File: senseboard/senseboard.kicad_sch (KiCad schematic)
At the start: 5 parts, among them U1 STM32L4Q5CGUx, U2 SHT4x, U3 SCD41-D-R2, U4 SGP41-D-R4, U5 TPS62840YBGR

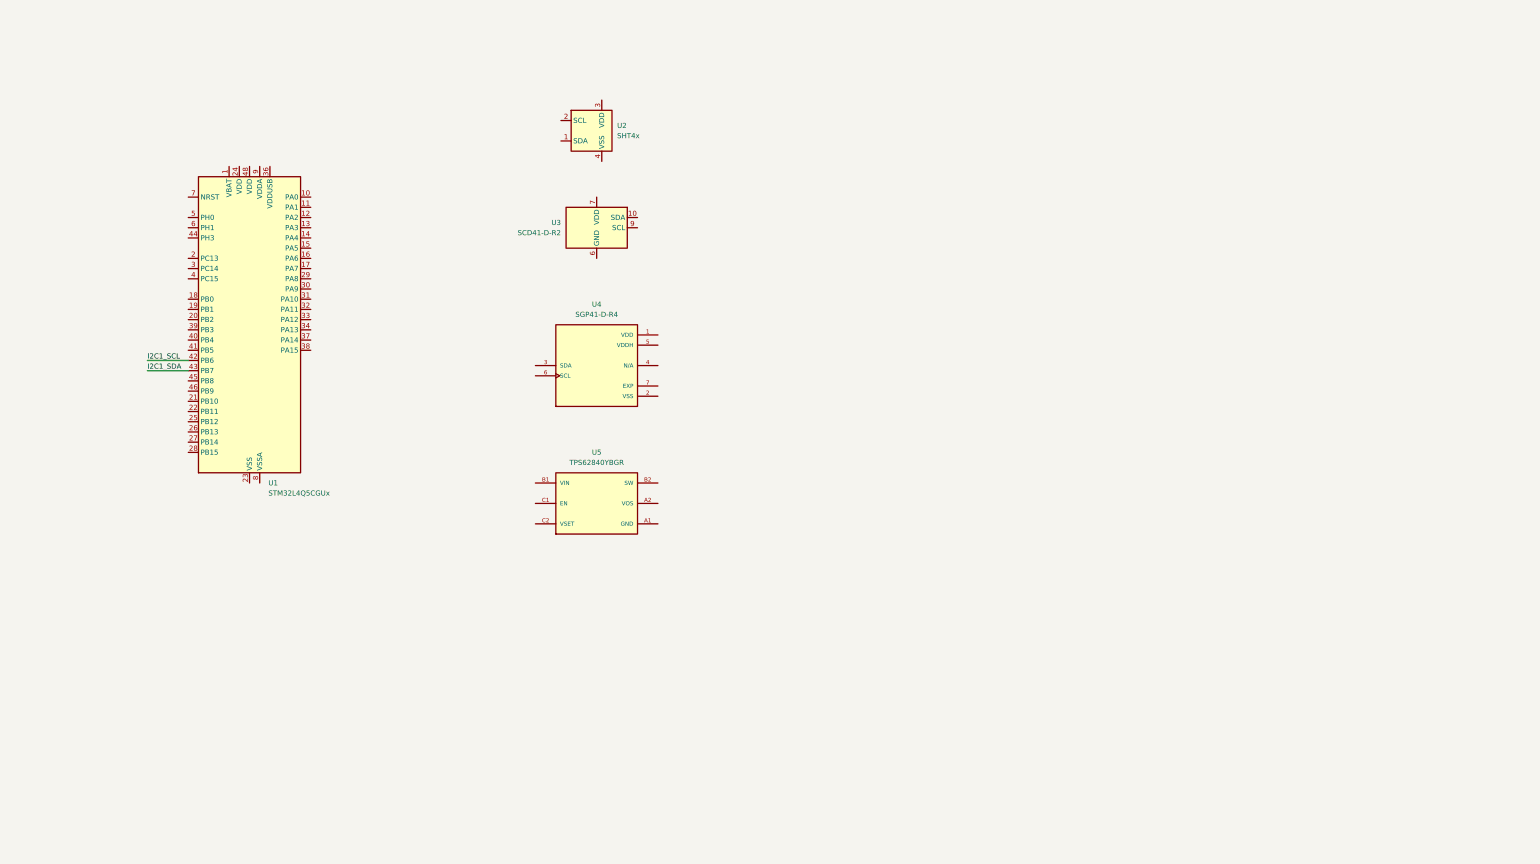
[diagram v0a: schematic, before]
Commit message: added updated regulators, power domains
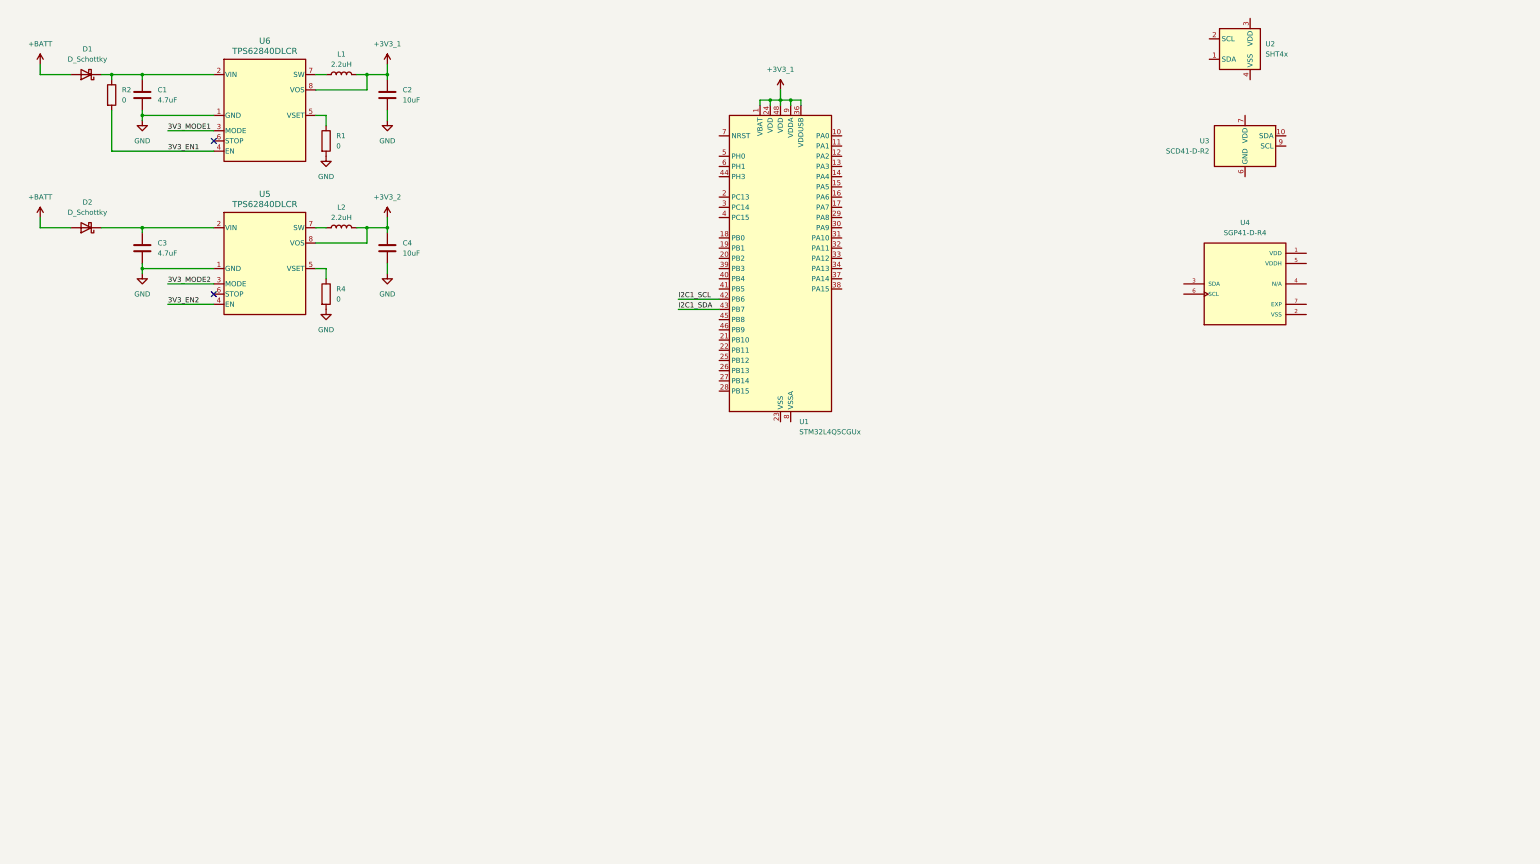
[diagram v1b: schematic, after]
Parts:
- removed U5: TPS62840YBGR, TPS62840YBGR:BGA6N40P3X2_146X96X50N, symbol TPS62840YBGR:TPS62840YBGR
- added C1, C3: 4.7uF, symbol Device:C
- added C2, C4: 10uF, symbol Device:C
- added D1, D2: D_Schottky, symbol Device:D_Schottky
- added L1, L2: 2.2uH, symbol Device:L
- added R1, R2, R4: 0, symbol Device:R
- added U5, U6: TPS62840DLCR, VSON8_2P1X1P6_TEX, symbol TPS62840DLCR:TPS62840DLCR
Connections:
- net +3V3_1: now reaches U1.1 (VBAT)
- net +3V3_1: now also U1.24 (VDD), U1.36 (VDDUSB), U1.48 (VDD), U1.9 (VDDA), C2.1, L1.2, U6.8 (VOS)
- new net: C1.1, D1.1 (K), R2.1, U6.2 (VIN)
- new net: L1.1, U6.7 (SW)
- new net: R1.1, U6.5 (VSET)
- new net: C3.1, D2.1 (K), U5.2 (VIN)
- new net: R4.1, U5.5 (VSET)
- new net: L2.1, U5.7 (SW)
- new net +3V3_2: C4.1, L2.2, U5.8 (VOS)
- new net +BATT: D1.2 (A), D2.2 (A)
- new net 3V3_EN1: R2.2, U6.4 (EN)
- new net 3V3_EN2: U5.4 (EN)
- new net 3V3_MODE1: U6.3 (MODE)
- new net 3V3_MODE2: U5.3 (MODE)
- new net GND: C1.2, C2.2, C3.2, C4.2, R1.2, R4.2, U5.1 (GND), U6.1 (GND)
- no-connect marks 0 -> 2
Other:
- moved on the sheet: U1, U2, U3, U4

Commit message: changed sheet size, added redundant sgp and worked to set up power domains further
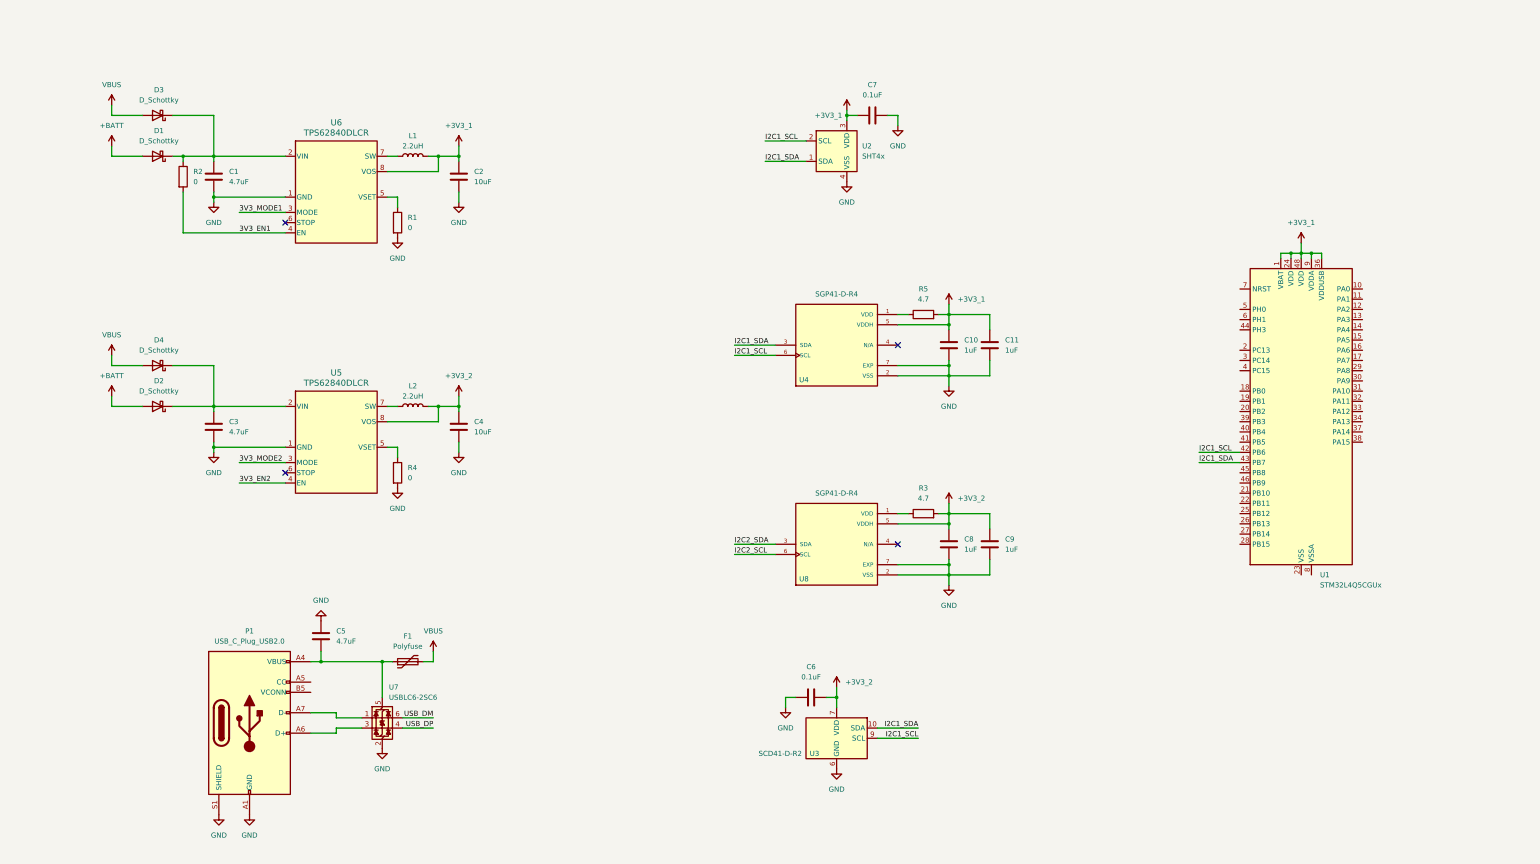
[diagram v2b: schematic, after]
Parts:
- added C10, C11, C8, C9: 1uF, symbol Device:C
- added C5: 4.7uF, symbol Device:C
- added C6, C7: 0.1uF, symbol Device:C
- added D3, D4: D_Schottky, symbol Device:D_Schottky
- added F1: Polyfuse, symbol Device:Polyfuse
- added P1: USB_C_Plug_USB2.0, symbol Connector:USB_C_Plug_USB2.0
- added R3, R5: 4.7, symbol Device:R
- added U7: USBLC6-2SC6, Package_TO_SOT_SMD:SOT-23-6, symbol Power_Protection:USBLC6-2SC6
- added U8: SGP41-D-R4, SGP41-D-R4:XDCR_SGP41-D-R4, symbol SGP41-D-R4:SGP41-D-R4
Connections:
- net +3V3_1: now also U2.3 (VDD), U4.5 (VDDH), C10.2, C11.2, C7.2, R5.2
- net +3V3_2: now also U3.19 (VDD), U3.7 (VDD), C6.2, C8.2, C9.2, R3.2, U8.5 (VDDH)
- net GND: now also U2.4 (VSS), U3.20 (GND), U3.21 (GND), U3.6 (GND), U4.2 (VSS), U4.7 (EXP), C10.1, C11.1, C5.1, C6.1, C7.1, C8.1, C9.1, P1.A1 (GND), P1.A12 (GND), P1.B1 (GND), P1.B12 (GND), P1.S1 (SHIELD), U7.2 (GND), U8.2 (VSS), U8.7 (EXP)
- net I2C1_SCL: now also U2.2 (SCL), U3.9 (SCL), U4.6 (SCL)
- net I2C1_SDA: now also U2.1 (SDA), U3.10 (SDA), U4.3 (SDA)
- net at C1.1, D1.1 (K), R2.1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: now also D3.1 (K)
- net at C3.1, D2.1 (K), U5.2 (VIN): now also D4.1 (K)
- net at U4.1 (VDD): now also R5.1
- new net: C5.2, F1.1, P1.A4 (VBUS), P1.A9 (VBUS), P1.B4 (VBUS), P1.B9 (VBUS), U7.5 (VBUS)
- new net: P1.A7 (D-), U7.1 (I/O1)
- new net: P1.A6 (D+), U7.3 (I/O2)
- new net: R3.1, U8.1 (VDD)
- new net I2C2_SCL: U8.6 (SCL)
- new net I2C2_SDA: U8.3 (SDA)
- new net USB_DM: U7.6 (I/O1)
- new net USB_DP: U7.4 (I/O2)
- new net VBUS: D3.2 (A), D4.2 (A), F1.2
- no-connect marks 2 -> 4
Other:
- company: (none) -> California Polytechnic State University, San Luis Obispo
- title: (none) -> Fire Detection on Campus Using AI - SENSEBOARD 1
- moved on the sheet: C1, C2, C3, C4, D1, D2, L1, L2, R1, R2, R4, U1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

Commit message: added LORA module, sd card, usb c filtering, stm32 neccesary reset/clocks and added ADC dividers and i2c pull ups
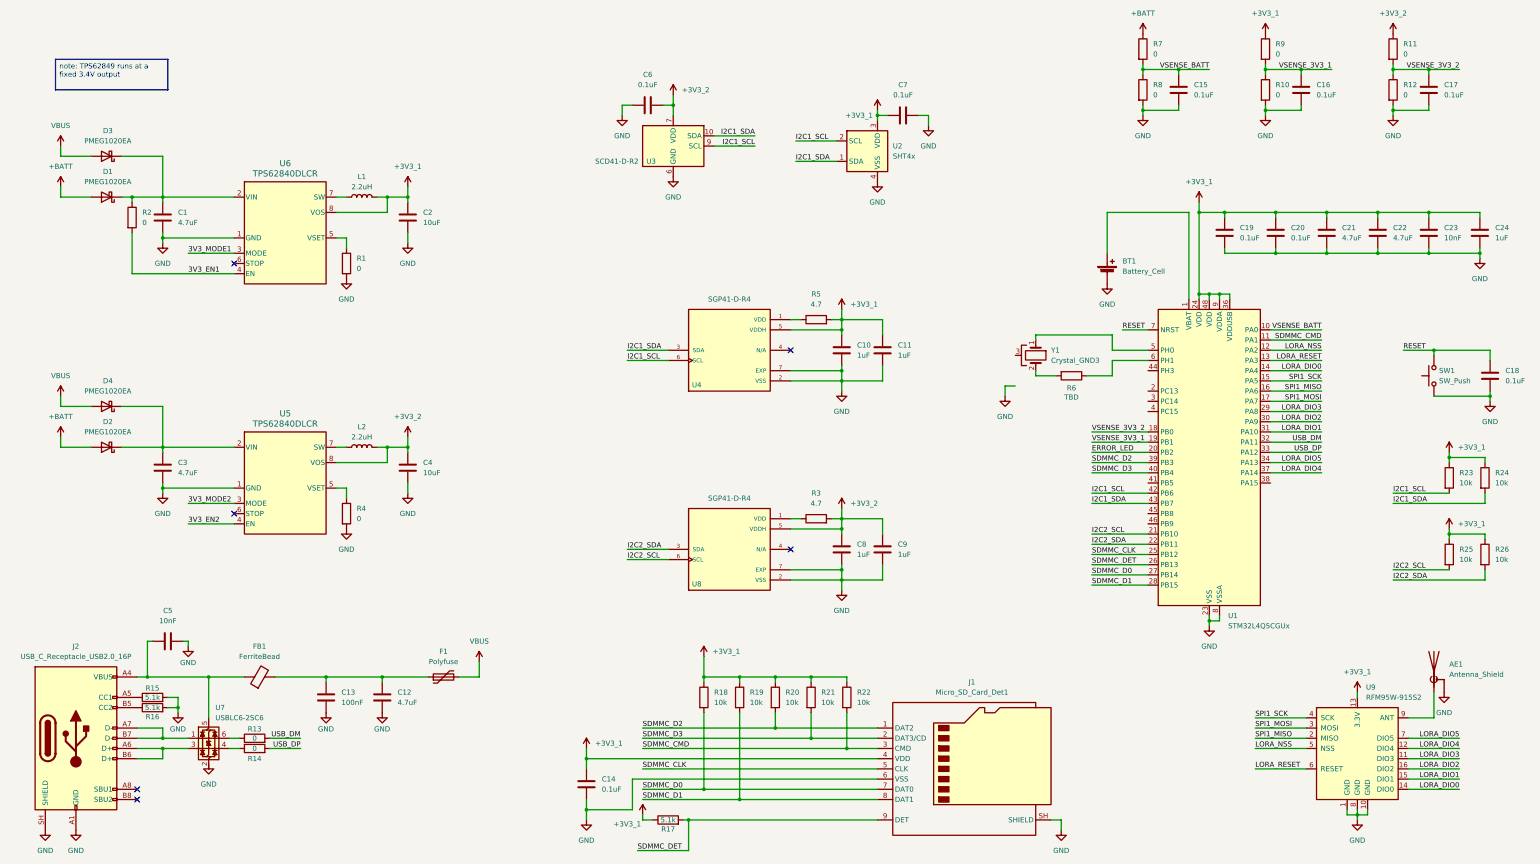
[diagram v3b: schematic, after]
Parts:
- removed P1: USB_C_Plug_USB2.0, symbol Connector:USB_C_Plug_USB2.0
- added AE1: Antenna_Shield, symbol Device:Antenna_Shield
- added BT1: Battery_Cell, symbol Device:Battery_Cell
- added C12, C21, C22: 4.7uF, symbol Device:C
- added C13: 100nF, symbol Device:C
- added C14, C15, C16, C17, C18, C19, C20: 0.1uF, symbol Device:C
- added C23: 10nF, symbol Device:C
- added C24: 1uF, symbol Device:C
- added FB1: FerriteBead, symbol Device:FerriteBead
- added J1: Micro_SD_Card_Det1, symbol Connector:Micro_SD_Card_Det1
- added J2: USB_C_Receptacle_USB2.0_16P, symbol Connector:USB_C_Receptacle_USB2.0_16P
- added R10, R11, R12, R13, R14, R7, R8, R9: 0, symbol Device:R
- added R15, R16, R17: 5.1k, symbol Device:R
- added R18, R19, R20, R21, R22, R23, R24, R25, R26: 10k, symbol Device:R
- added R6: TBD, symbol Device:R
- added SW1: SW_Push, symbol Switch:SW_Push
- added U9: RFM95W-915S2, symbol RF_Module:RFM95W-915S2
- added Y1: Crystal_GND3, symbol Device:Crystal_GND3
- C5: value 4.7uF -> 10nF
- D1, D2, D3, D4: value D_Schottky -> PMEG1020EA
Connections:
- net +3V3_1: now also C14.2, C19.2, C20.2, C21.2, C22.2, C23.2, C24.2, J1.4 (VDD), R17.1, R18.1, R19.1, R20.1, R21.1, R22.1, R23.1, R24.1, R25.1, R26.1, R9.1, U9.13 (3.3V); no longer U1.1 (VBAT)
- net +3V3_2: now also R11.1
- net +BATT: now also R7.1
- net GND: now also C5.2, U1.23 (VSS), U1.35 (VSS), U1.47 (VSS), U1.49 (VSS), U1.8 (VSSA), AE1.2 (Shield), BT1.2 (-), C12.1, C13.1, C14.1, C15.2, C16.2, C17.2, C18.2, C19.1, C20.1, C21.1, C22.1, C23.1, C24.1, J1.6 (VSS), J1.SH (SHIELD), J2.A1 (GND), J2.A12 (GND), J2.B1 (GND), J2.B12 (GND), J2.SH (SHIELD), R10.2, R12.2, R15.2, R16.2, R8.2, SW1.1, U9.1 (GND), U9.10 (GND), U9.8 (GND); no longer C5.1, U7.2 (GND)
- net I2C1_SCL: now also R23.2
- net I2C1_SDA: now also R24.2
- net I2C2_SCL: now also U1.21 (PB10), R25.2
- net I2C2_SDA: now also U1.22 (PB11), R26.2
- net USB_DM: now also U1.32 (PA11), R13.2; no longer U7.6 (I/O1)
- net USB_DP: now also U1.33 (PA12), R14.2; no longer U7.4 (I/O2)
- net VSENSE_BATT: now reaches U1.10 (PA0)
- net VSENSE_BATT: now also C15.1, R7.2, R8.1
- net SDMMC_CMD: now reaches U1.11 (PA1)
- net SDMMC_CMD: now also J1.3 (CMD), R22.2
- net LORA_NSS: now reaches U1.12 (PA2)
- net LORA_NSS: now also U9.5 (NSS)
- net LORA_RESET: now reaches U1.13 (PA3)
- net LORA_RESET: now also U9.6 (RESET)
- net LORA_DIO0: now reaches U1.14 (PA4)
- net LORA_DIO0: now also U9.14 (DIO0)
- net SPI1_SCK: now reaches U1.15 (PA5)
- net SPI1_SCK: now also U9.4 (SCK)
- net SPI1_MISO: now reaches U1.16 (PA6)
- net SPI1_MISO: now also U9.2 (MISO)
- net SPI1_MOSI: now reaches U1.17 (PA7)
- net SPI1_MOSI: now also U9.3 (MOSI)
- net VSENSE_3V3_2: now reaches U1.18 (PB0)
- net VSENSE_3V3_2: now also C17.1, R11.2, R12.1
- net VSENSE_3V3_1: now reaches U1.19 (PB1)
- net VSENSE_3V3_1: now also C16.1, R10.1, R9.2
- net ERROR_LED: now reaches U1.20 (PB2)
- net SDMMC_CLK: now reaches U1.25 (PB12)
- net SDMMC_CLK: now also J1.5 (CLK)
- net SDMMC_DET: now reaches U1.26 (PB13)
- net SDMMC_DET: now also J1.9 (DET), R17.2
- net SDMMC_D0: now reaches U1.27 (PB14)
- net SDMMC_D0: now also J1.7 (DAT0), R18.2
- net SDMMC_D1: now reaches U1.28 (PB15)
- net SDMMC_D1: now also J1.8 (DAT1), R19.2
- net LORA_DIO3: now reaches U1.29 (PA8)
- net LORA_DIO3: now also U9.11 (DIO3)
- net LORA_DIO2: now reaches U1.30 (PA9)
- net LORA_DIO2: now also U9.16 (DIO2)
- net LORA_DIO1: now reaches U1.31 (PA10)
- net LORA_DIO1: now also U9.15 (DIO1)
- net LORA_DIO5: now reaches U1.34 (PA13)
- net LORA_DIO5: now also U9.7 (DIO5)
- net LORA_DIO4: now reaches U1.37 (PA14)
- net LORA_DIO4: now also U9.12 (DIO4)
- net SDMMC_D2: now reaches U1.39 (PB3)
- net SDMMC_D2: now also J1.1 (DAT2), R20.2
- net SDMMC_D3: now reaches U1.40 (PB4)
- net SDMMC_D3: now also J1.2 (DAT3/CD), R21.2
- net at U1.5 (PH0): now also Y1.1
- net at U1.6 (PH1): now also R6.1
- net RESET: now reaches U1.7 (NRST)
- net RESET: now also C18.1, SW1.2
- net at U7.1 (I/O1): now also J2.A7 (D-), J2.B7 (D-)
- net at U7.3 (I/O2): now also J2.A6 (D+), J2.B6 (D+)
- new net: R13.1, U7.6 (I/O1)
- new net: R6.2, Y1.2
- new net: C5.1, FB1.1, J2.A4 (VBUS), J2.A9 (VBUS), J2.B4 (VBUS), J2.B9 (VBUS), U7.5 (VBUS)
- new net: J2.A5 (CC1), R15.1
- new net: C12.2, C13.2, F1.1, FB1.2
- new net: R14.1, U7.4 (I/O2)
- new net: BT1.1 (+), U1.1 (VBAT)
- new net: AE1.1 (A), U9.9 (ANT)
- new net: J2.B5 (CC2), R16.1
- no-connect marks 4 -> 6
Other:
- moved on the sheet: C1, C10, C11, C2, C3, C4, C5, C6, C7, C8, C9, D1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
